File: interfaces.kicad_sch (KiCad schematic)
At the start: 91 parts, among them IC3 TPD8S009DSMR, J6 685119134923, J7 693071020811, J9 USB4105-GF-A, Q1 BSS138APW, Q10 BSS138APW, Q2 BSS138APW, Q3 BSS138APW, Q4 BSS138APW, Q5 BSS138APW, Q6 BSS138APW, Q9 BSS138APW, U7 FT4232HQ, Y2 ABM8G-12.000MHZ-18-D2Y-T

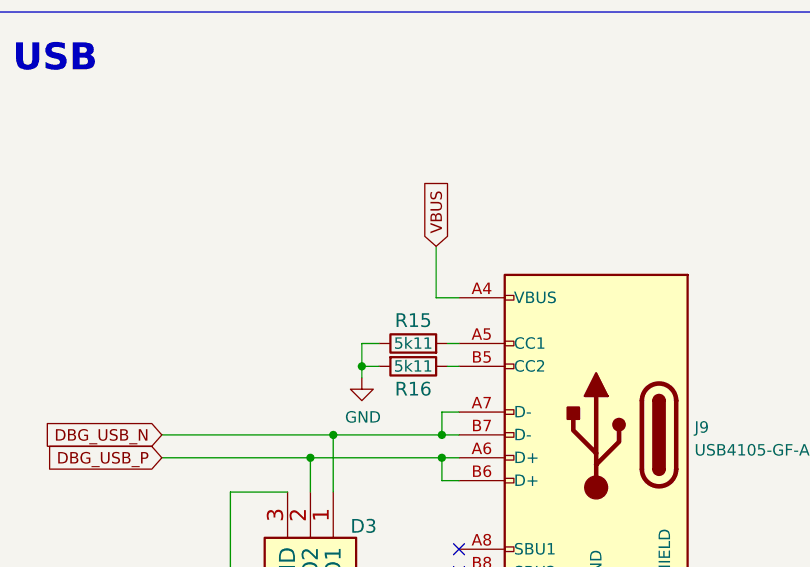
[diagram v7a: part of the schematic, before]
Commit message: Assign and connect misc. signals. Add, place and route decoupling capacitors
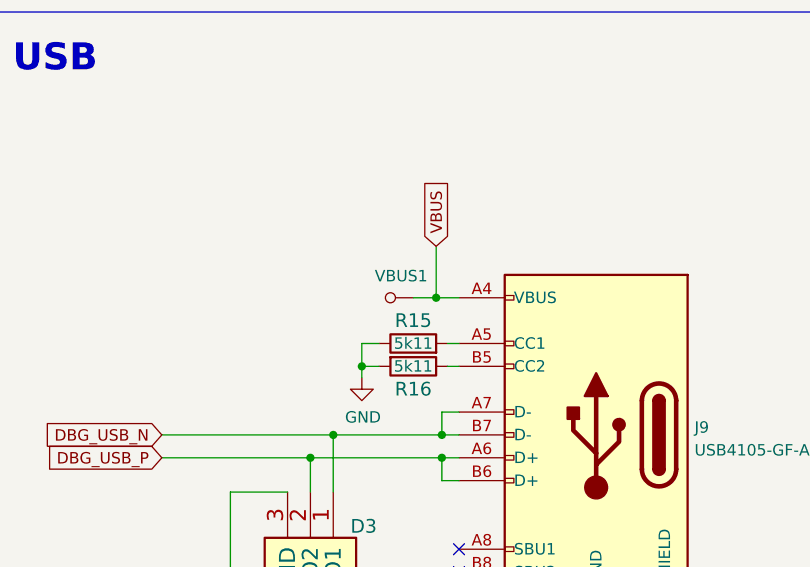
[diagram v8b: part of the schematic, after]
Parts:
- added VBUS1: TP_SMD1MM, data-center-dram-tester-footprints:Testpoint_smd_1mm, symbol data-center-dram-tester:TP_SMD1MM
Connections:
- net VBUS: now also VBUS1.1
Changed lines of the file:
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@@
   (junction (at 268.605 204.47) (diameter 0) (color 0 0 0 0)
   )
+  (junction (at 243.205 152.4) (diameter 0) (color 0 0 0 0)
+  )
   (junction (at 78.105 76.2) (diameter 0) (color 0 0 0 0)
   )
@@
     (stroke (width 0) (type default) (color 0 0 0 0))
   )
+  (wire (pts (xy 240.665 152.4) (xy 243.205 152.4))
+    (stroke (width 0) (type default) (color 0 0 0 0))
+  )
   (wire (pts (xy 339.725 49.53) (xy 339.725 45.085))
     (stroke (width 0) (type default) (color 0 0 0 0))
@@
     (pin "3")
   )
+  (symbol (lib_id "data-center-dram-tester:TP_SMD1MM") (at 238.125 152.4 270) (unit 1)
+    (in_bom yes) (on_board yes)
+    (property "Reference" "VBUS1" (id 0) (at 239.3188 149.987 90))
+    (property "Value" "TP_SMD1MM" (id 1) (at 235.585 152.4 0)
+      (effects (font (size 1.27 1.27)) hide)
+    )
+    (property "Footprint" "data-center-dram-tester-footprints:Testpoint_smd_1mm" (id 2) (at 243.205 157.48 0)
+      (effects (font (size 1.524 1.524)) (justify left) hide)
+    )
+    (property "Datasheet" "" (id 3) (at 245.745 157.48 0)
+      (effects (font (size 1.524 1.524)) (justify left) hide)
+    )
+    (pin "1")
+  )
   (symbol (lib_id "data-center-dram-tester:GND") (at 177.8 266.065 0) (unit 1)
